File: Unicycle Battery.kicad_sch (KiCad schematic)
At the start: 0 parts

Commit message: PCB Guestimate complete (tm)
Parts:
- added BT1, BT10, BT11, BT12, BT2, BT3, BT4, BT5, BT6, BT7, BT8, BT9: ~, Unicycle:P Group, symbol Unicycle:Batt
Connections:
- new net: BT10.+, BT11.-
- new net: BT10.-, BT9.+
- new net: BT4.+, BT5.-
- new net: BT3.+, BT4.-
- new net: BT1.+, BT2.-
- new net: BT11.+, BT12.-
- new net: BT2.+, BT3.-
- new net: BT8.+, BT9.-
- new net: BT7.+, BT8.-
- new net: BT6.+, BT7.-
- new net: BT5.+, BT6.-
- new net +BATT: BT12.+
- new net -BATT: BT1.-

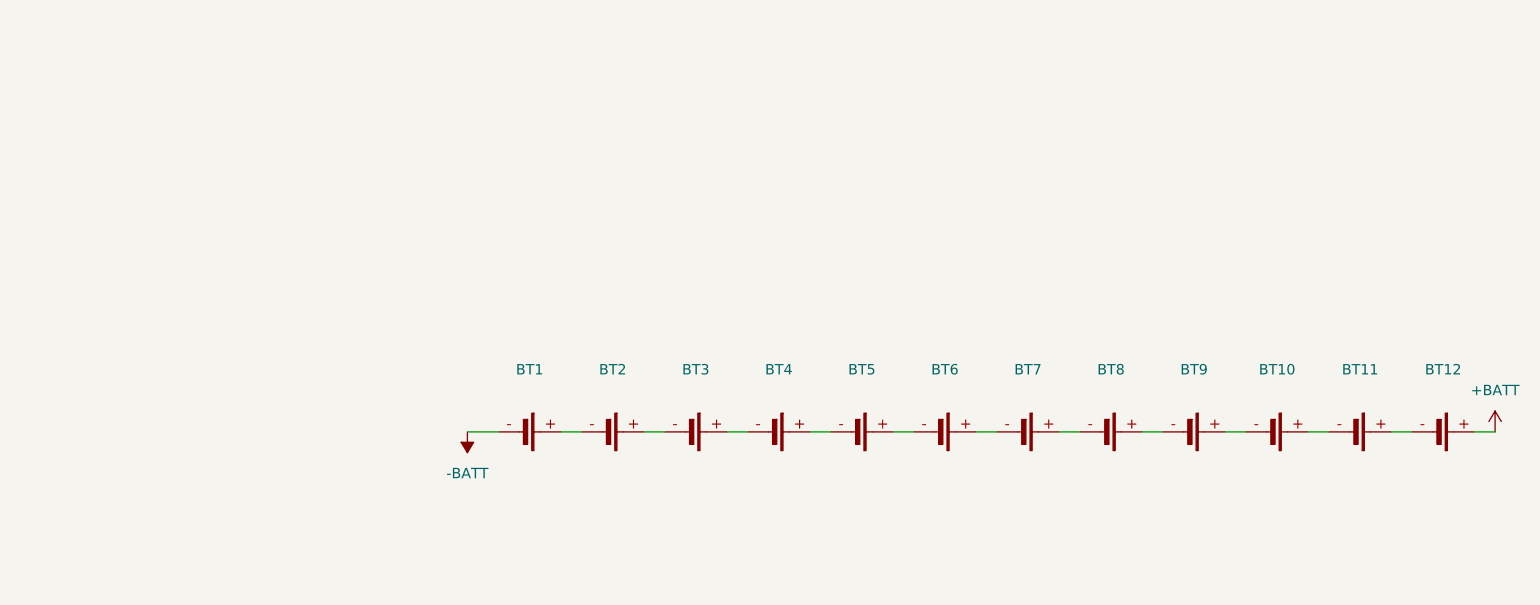
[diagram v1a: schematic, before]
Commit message: First draft
Done:
One pad per connection
Alignment done
All components added

TODO:
Via stitching
Clean up traces + increase width
Remove or stitch top layer pads
Double check math
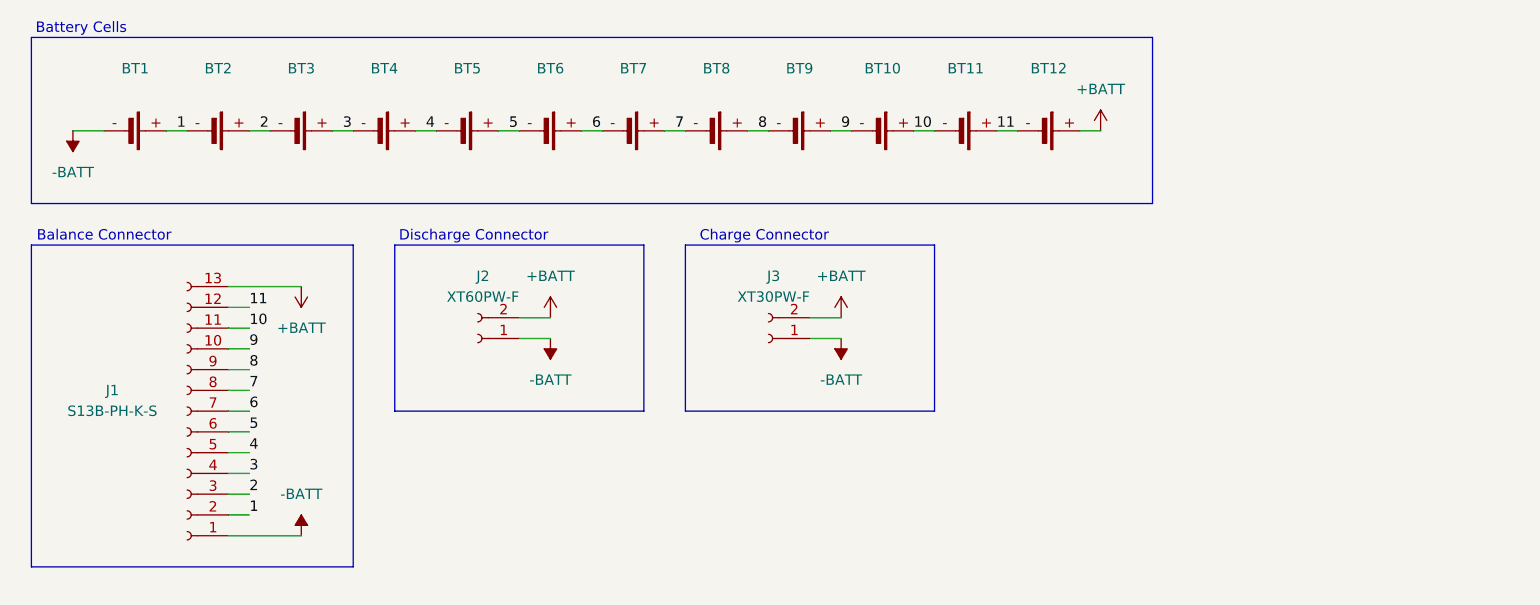
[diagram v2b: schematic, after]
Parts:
- added J1: S13B-PH-K-S, Connector_JST:JST_PH_S13B-PH-K_1x13_P2.00mm_Horizontal, symbol Connector:Conn_01x13_Socket
- added J2: XT60PW-F, Connector_AMASS:AMASS_XT60PW-F_1x02_P7.20mm_Horizontal, symbol Connector:Conn_01x02_Socket
- added J3: XT30PW-F, Connector_AMASS:AMASS_XT30PW-F_1x02_P2.50mm_Horizontal, symbol Connector:Conn_01x02_Socket
- BT1, BT2, BT7, BT8: footprint Unicycle:P Group -> Unicycle:P Group Even
- BT10, BT3, BT4: footprint Unicycle:P Group -> Unicycle:P Group End
- BT11, BT5: footprint Unicycle:P Group -> Unicycle:P Group 4-5 10-11
- BT12, BT6: footprint Unicycle:P Group -> Unicycle:P Group 5-6 11-+
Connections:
- net +BATT: now also J1.13 (Pin_13), J2.2 (Pin_2), J3.2 (Pin_2)
- net -BATT: now also J1.1 (Pin_1), J2.1 (Pin_1), J3.1 (Pin_1)
- net 10: now reaches BT10.+, BT11.-
- net 10: now also J1.11 (Pin_11)
- net 9: now reaches BT10.-, BT9.+
- net 9: now also J1.10 (Pin_10)
- net 4: now reaches BT4.+, BT5.-
- net 4: now also J1.5 (Pin_5)
- net 3: now reaches BT3.+, BT4.-
- net 3: now also J1.4 (Pin_4)
- net 1: now reaches BT1.+, BT2.-
- net 1: now also J1.2 (Pin_2)
- net 11: now reaches BT11.+, BT12.-
- net 11: now also J1.12 (Pin_12)
- net 2: now reaches BT2.+, BT3.-
- net 2: now also J1.3 (Pin_3)
- net 8: now reaches BT8.+, BT9.-
- net 8: now also J1.9 (Pin_9)
- net 7: now reaches BT7.+, BT8.-
- net 7: now also J1.8 (Pin_8)
- net 6: now reaches BT6.+, BT7.-
- net 6: now also J1.7 (Pin_7)
- net 5: now reaches BT5.+, BT6.-
- net 5: now also J1.6 (Pin_6)
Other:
- note added: "Balance Connector"
- note added: "Battery Cells"
- note added: "Charge Connector"
- note added: "Discharge Connector"
- title: (none) -> Unicycle Battery PCB
- moved on the sheet: BT1, BT10, BT11, BT12, BT2, BT3, BT4, BT5, BT6, BT7, BT8, BT9

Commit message: Finished PCB
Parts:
- added H1, H2: MountingHole, MountingHole:MountingHole_4.3mm_M4, symbol Mechanical:MountingHole
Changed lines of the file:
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@@
+	)
+	(symbol
+		(lib_id "Mechanical:MountingHole")
+		(at 85.09 90.17 0)
+		(unit 1)
+		(exclude_from_sim no)
+		(in_bom no)
+		(on_board yes)
+		(dnp no)
+		(fields_autoplaced yes)
+		(property "Reference" "H1"
+			(at 87.63 88.8999 0)
+			(effects
+				(font
+					(size 1.27 1.27)
+				)
+				(justify left)
+			)
+		)
+		(property "Value" "MountingHole"
+			(at 87.63 91.4399 0)
+			(effects
+				(font
+					(size 1.27 1.27)
+				)
+				(justify left)
+			)
+		)
+		(property "Footprint" "MountingHole:MountingHole_4.3mm_M4"
+			(at 85.09 90.17 0)
+			(effects
+				(font
+					(size 1.27 1.27)
+				)
+				(hide yes)
+			)
+		)
+		(property "Datasheet" "~"
+			(at 85.09 90.17 0)
+			(effects
+				(font
+					(size 1.27 1.27)
+				)
+				(hide yes)
+			)
+		)
+		(property "Description" "Mounting Hole without connection"
+			(at 85.09 90.17 0)
+			(effects
+				(font
+					(size 1.27 1.27)
+				)
+				(hide yes)
+			)
+		)
+		(instances
+			(project ""
+				(path "/d1cd8537-56f0-4291-8d25-fe29b385b4b9"
+					(reference "H1")
+					(unit 1)
+				)
+			)
+		)
 	)
 	(symbol
@@
 					(unit 1)
 				)
+			)
+		)
+	)
+	(symbol
+		(lib_id "Mechanical:MountingHole")
+		(at 105.41 90.17 0)
+		(unit 1)
+		(exclude_from_sim no)
+		(in_bom no)
+		(on_board yes)
+		(dnp no)
+		(fields_autoplaced yes)
+		(property "Reference" "H2"
+			(at 107.95 88.8999 0)
+			(effects
+				(font
+					(size 1.27 1.27)
+				)
+				(justify left)
+			)
+		)
+		(property "Value" "MountingHole"
+			(at 107.95 91.4399 0)
+			(effects
+				(font
+					(size 1.27 1.27)
+				)
+				(justify left)
+			)
+		)
+		(property "Footprint" "MountingHole:MountingHole_4.3mm_M4"
+			(at 105.41 90.17 0)
+			(effects
+				(font
+					(size 1.27 1.27)
+				)
+				(hide yes)
+			)
+		)
+		(property "Datasheet" "~"
+			(at 105.41 90.17 0)
+			(effects
+				(font
+					(size 1.27 1.27)
+				)
+				(hide yes)
+			)
+		)
+		(property "Description" "Mounting Hole without connection"
+			(at 105.41 90.17 0)
+			(effects
+				(font
+					(size 1.27 1.27)
+				)
+				(hide yes)
+			)
+		)
+		(instances
+			(project "Unicycle Battery"
+				(path "/d1cd8537-56f0-4291-8d25-fe29b385b4b9"
+					(reference "H2")
+					(unit 1)
+				)
